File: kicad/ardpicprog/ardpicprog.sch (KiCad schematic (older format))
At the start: 33 parts, among them P1 CONN_01X06, P2 CONN_01X02, Q1 BC548, SW1 SW_PUSH, U1 PIC16F627, U2 MC34063, U3 LM78L12ACZ

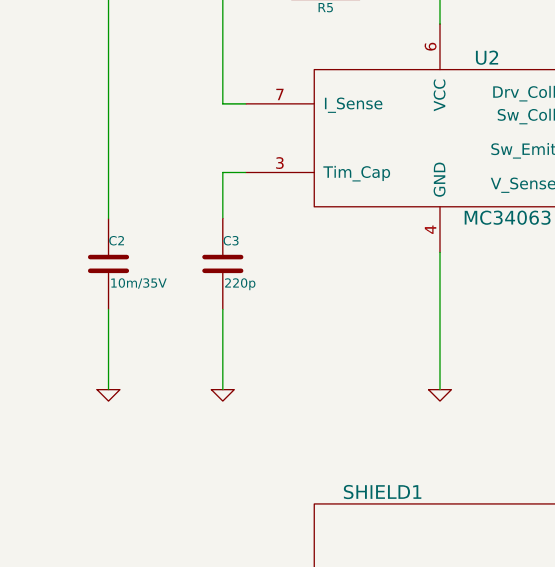
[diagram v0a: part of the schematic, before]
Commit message: update c2 to 10u/6.3V on 5V line
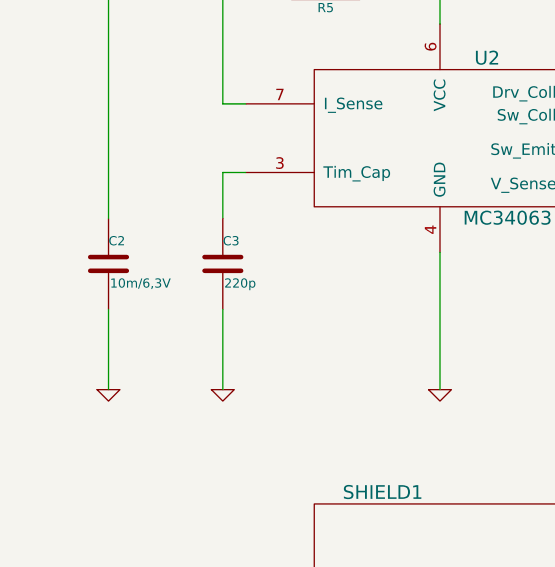
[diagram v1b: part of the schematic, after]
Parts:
- C2: value 10m/35V -> 10m/6,3V
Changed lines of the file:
@@
 P 1000 2450
 F 0 "C2" H 1000 2550 40  0000 L CNN
-F 1 "10m/35V" H 1006 2365 40  0000 L CNN
+F 1 "10m/6,3V" H 1006 2365 40  0000 L CNN
 F 2 "" H 1038 2300 30  0000 C CNN
 F 3 "" H 1000 2450 60  0000 C CNN

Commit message: same changes
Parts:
- C1, C2, C3, C4, C5, C6, C7: symbol C -> C-RESCUE-ardpicprog
- R1, R10, R11, R2, R3, R4, R5, R6, R7, R8, R9: symbol R -> R-RESCUE-ardpicprog
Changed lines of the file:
@@
 EESchema Schematic File Version 2
+LIBS:ardpicprog-rescue
 LIBS:power
 LIBS:device
@@
 LIBS:memory
 LIBS:xilinx
-LIBS:special
 LIBS:microcontrollers
 LIBS:dsp
@@
 $EndComp
 $Comp
-L GND #PWR01
+L GND-RESCUE-ardpicprog #PWR01
 U 1 1 543FB4F0
 P 1350 7500
@@
 $EndComp
 $Comp
-L GND #PWR02
+L GND-RESCUE-ardpicprog #PWR02
 U 1 1 543FB522
 P 4800 7300
@@
 $EndComp
 $Comp
-L C C1
+L C-RESCUE-ardpicprog C1
 U 1 1 543FBBF4
 P 8100 1450
@@
 $EndComp
 $Comp
-L GND #PWR03
+L GND-RESCUE-ardpicprog #PWR03
 U 1 1 543FBCBB
 P 8100 1800
@@
 PGM
 $Comp
-L GND #PWR04
+L GND-RESCUE-ardpicprog #PWR04
 U 1 1 543FC550
 P 9700 1200
@@
 PGM
 $Comp
-L R R4
+L R-RESCUE-ardpicprog R4
 U 1 1 543FCB5E
 P 9950 5850
@@
 $EndComp
 $Comp
-L GND #PWR05
+L GND-RESCUE-ardpicprog #PWR05
 U 1 1 543FCBB3
 P 9950 6200
@@
 MCLR(A1)
 $Comp
-L R R3
+L R-RESCUE-ardpicprog R3
 U 1 1 543FCC61
 P 9950 2550
@@
 $EndComp
 $Comp
-L R R1
+L R-RESCUE-ardpicprog R1
 U 1 1 543FCDA2
 P 9300 3200
@@
 $EndComp
 $Comp
-L GND #PWR06
+L GND-RESCUE-ardpicprog #PWR06
 U 1 1 543FCF51
 P 9950 3550
@@
 ACTIVITY(A5)
 $Comp
-L R R2
+L R-RESCUE-ardpicprog R2
 U 1 1 543FEABB
 P 9300 3850
@@
 $EndComp
 $Comp
-L GND #PWR07
+L GND-RESCUE-ardpicprog #PWR07
 U 1 1 543FEB21
 P 9950 4350
@@
 RESET
 $Comp
-L GND #PWR08
+L GND-RESCUE-ardpicprog #PWR08
 U 1 1 543FED57
 P 9950 5100
@@
 DATA(D7)
 $Comp
-L R R9
+L R-RESCUE-ardpicprog R9
 U 1 1 544037E6
 P 10400 2200
@@
 $EndComp
 $Comp
-L GND #PWR09
+L GND-RESCUE-ardpicprog #PWR09
 U 1 1 54403990
 P 11000 2950
@@
 $EndComp
 $Comp
-L GND #PWR010
+L GND-RESCUE-ardpicprog #PWR010
 U 1 1 5440477D
 P 1350 4400
@@
 5V
 $Comp
-L GND #PWR011
+L GND-RESCUE-ardpicprog #PWR011
 U 1 1 54404FEC
 P 3700 3750
@@
 5V
 $Comp
-L GND #PWR012
+L GND-RESCUE-ardpicprog #PWR012
 U 1 1 54406760
 P 2450 3000
@@
 $EndComp
 $Comp
-L GND #PWR013
+L GND-RESCUE-ardpicprog #PWR013
 U 1 1 5440682B
 P 3550 2000
@@
 $EndComp
 $Comp
-L R R7
+L R-RESCUE-ardpicprog R7
 U 1 1 54406898
 P 3400 2500
@@
 $EndComp
 $Comp
-L R R8
+L R-RESCUE-ardpicprog R8
 U 1 1 544068DB
 P 4000 2100
@@
 $EndComp
 $Comp
-L GND #PWR014
+L GND-RESCUE-ardpicprog #PWR014
 U 1 1 54406A7C
 P 3400 3000
@@
 $EndComp
 $Comp
-L C C4
+L C-RESCUE-ardpicprog C4
 U 1 1 54406B81
 P 4350 2500
@@
 $EndComp
 $Comp
-L GND #PWR015
+L GND-RESCUE-ardpicprog #PWR015
 U 1 1 54406BE7
 P 4350 3000
@@
 $EndComp
 $Comp
-L R R6
+L R-RESCUE-ardpicprog R6
 U 1 1 54407870
 P 3400 1350
@@
 $EndComp
 $Comp
-L C C3
+L C-RESCUE-ardpicprog C3
 U 1 1 54407D45
 P 1500 2450
@@
 $EndComp
 $Comp
-L GND #PWR016
+L GND-RESCUE-ardpicprog #PWR016
 U 1 1 54407F9B
 P 1500 3000
@@
 $EndComp
 $Comp
-L C C2
+L C-RESCUE-ardpicprog C2
 U 1 1 54408434
 P 1000 2450
@@
 $EndComp
 $Comp
-L GND #PWR017
+L GND-RESCUE-ardpicprog #PWR017
 U 1 1 544084F8
 P 1000 3000
@@
 $EndComp
 $Comp
-L R R5
+L R-RESCUE-ardpicprog R5
 U 1 1 54408974
 P 1950 1250
@@
 13V
 $Comp
-L C C6
+L C-RESCUE-ardpicprog C6
 U 1 1 5440F98F
 P 5850 4250
@@
 $EndComp
 $Comp
-L C C7
+L C-RESCUE-ardpicprog C7
 U 1 1 5440FB1D
 P 6800 4300
@@
 $EndComp
 $Comp
-L R R11
+L R-RESCUE-ardpicprog R11
 U 1 1 5440FB9B
 P 6800 4600
@@
 $EndComp
 $Comp
-L R R10
+L R-RESCUE-ardpicprog R10
 U 1 1 5440FC8D
 P 6450 4950
@@
 	5850 4450 5850 4600
 $Comp
-L GND #PWR018
+L GND-RESCUE-ardpicprog #PWR018
 U 1 1 54410DD3
 P 6450 5400
@@
 	6450 5400 6450 5200
 $Comp
-L GND #PWR019
+L GND-RESCUE-ardpicprog #PWR019
 U 1 1 54410F12
 P 5200 4350
@@
 	5200 4000 5150 4000
 $Comp
-L C C5
+L C-RESCUE-ardpicprog C5
 U 1 1 544119A7
 P 5500 4250
@@
 Connection ~ 5500 3900
 $Comp
-L GND #PWR020
+L GND-RESCUE-ardpicprog #PWR020
 U 1 1 54411B0A
 P 5500 4600

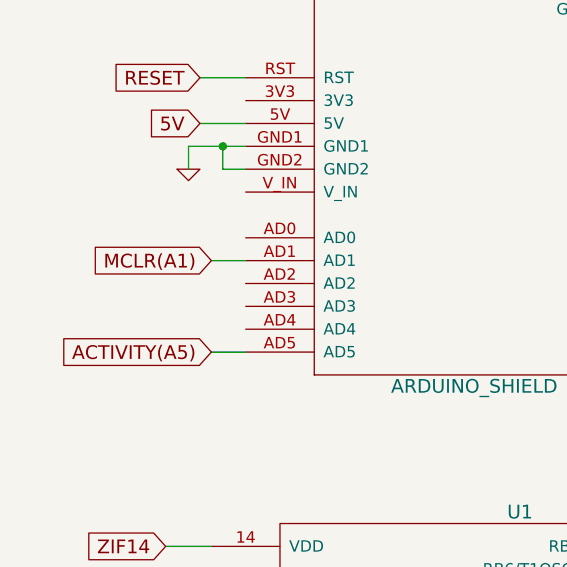
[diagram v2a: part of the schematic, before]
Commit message: VDD d2 connection fix
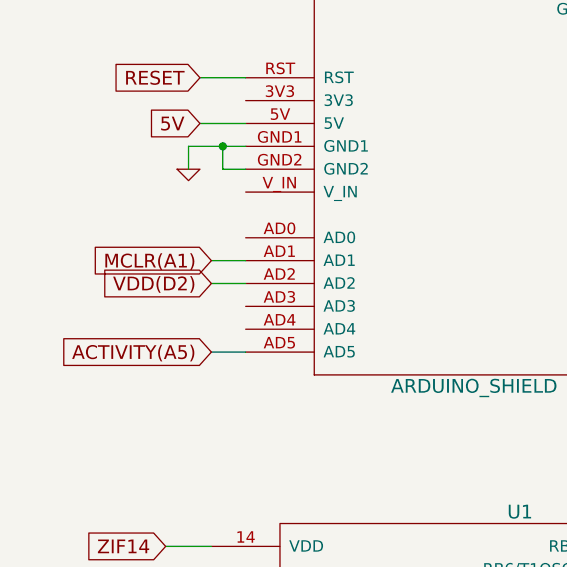
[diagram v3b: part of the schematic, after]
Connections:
- net VDD(D2): now also SHIELD1.AD2
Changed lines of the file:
@@
 Wire Wire Line
 	7750 3900 7700 3900
+Text GLabel 1450 4900 0    60   Input ~ 0
+VDD(D2)
+Wire Wire Line
+	1600 4900 1450 4900
 $EndSCHEMATC

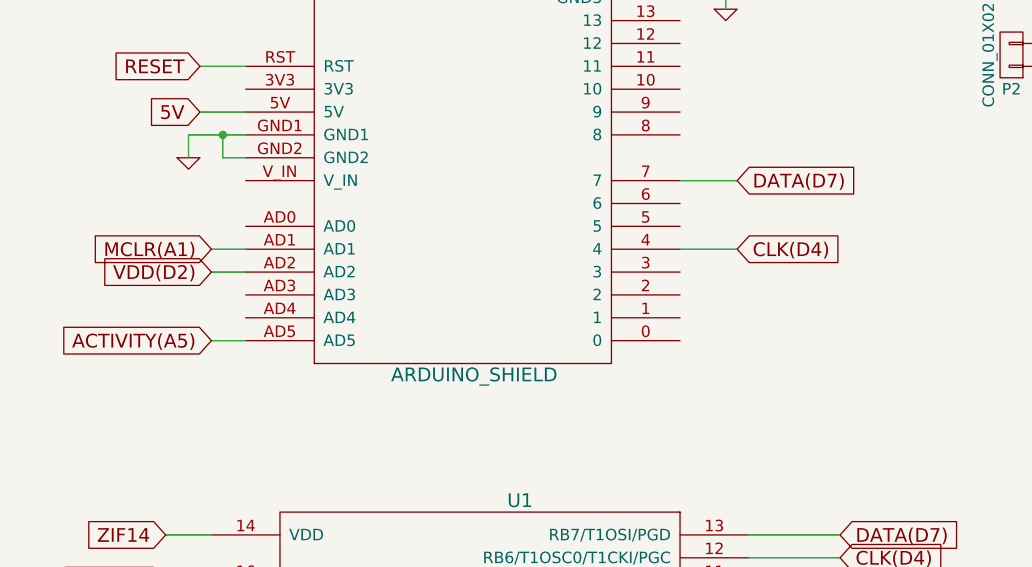
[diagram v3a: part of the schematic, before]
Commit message: VDD d2 connection fix
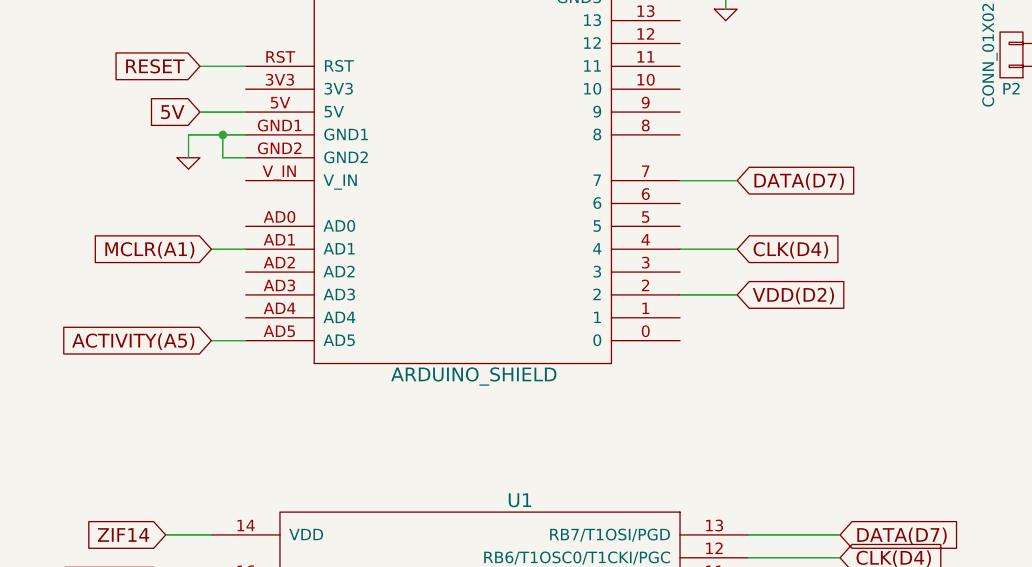
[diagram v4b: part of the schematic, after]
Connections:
- net VDD(D2): now also SHIELD1.2; no longer SHIELD1.AD2
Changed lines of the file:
@@
 Wire Wire Line
 	7750 3900 7700 3900
-Text GLabel 1450 4900 0    60   Input ~ 0
+Text GLabel 3750 5000 2    60   Input ~ 0
 VDD(D2)
 Wire Wire Line
-	1600 4900 1450 4900
+	3750 5000 3500 5000
 $EndSCHEMATC
